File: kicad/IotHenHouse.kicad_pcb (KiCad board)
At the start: 2 copper layers, 55.9 x 80.9 mm, 60 parts, among them J1 GND NC 5V RXD TXD NC, J2 Conn_01x02_Female, J3 3.3V SW1 SW2, M1 + MOT -, SW0 RESET, SW1 FLASH, U1 LM7805_TO220, U2 ESP-12E, U3 L298P, U4 LM1117-3.3

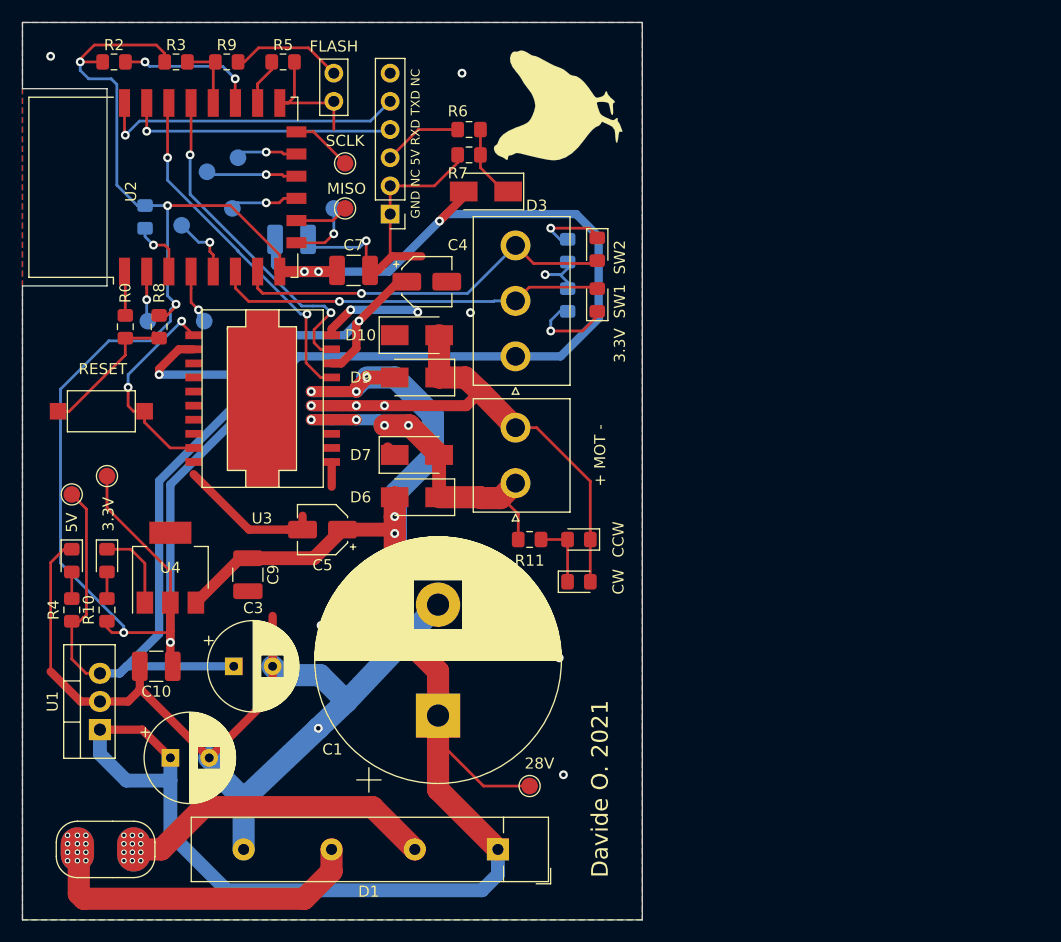
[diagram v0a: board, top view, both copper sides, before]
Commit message: mounting holes
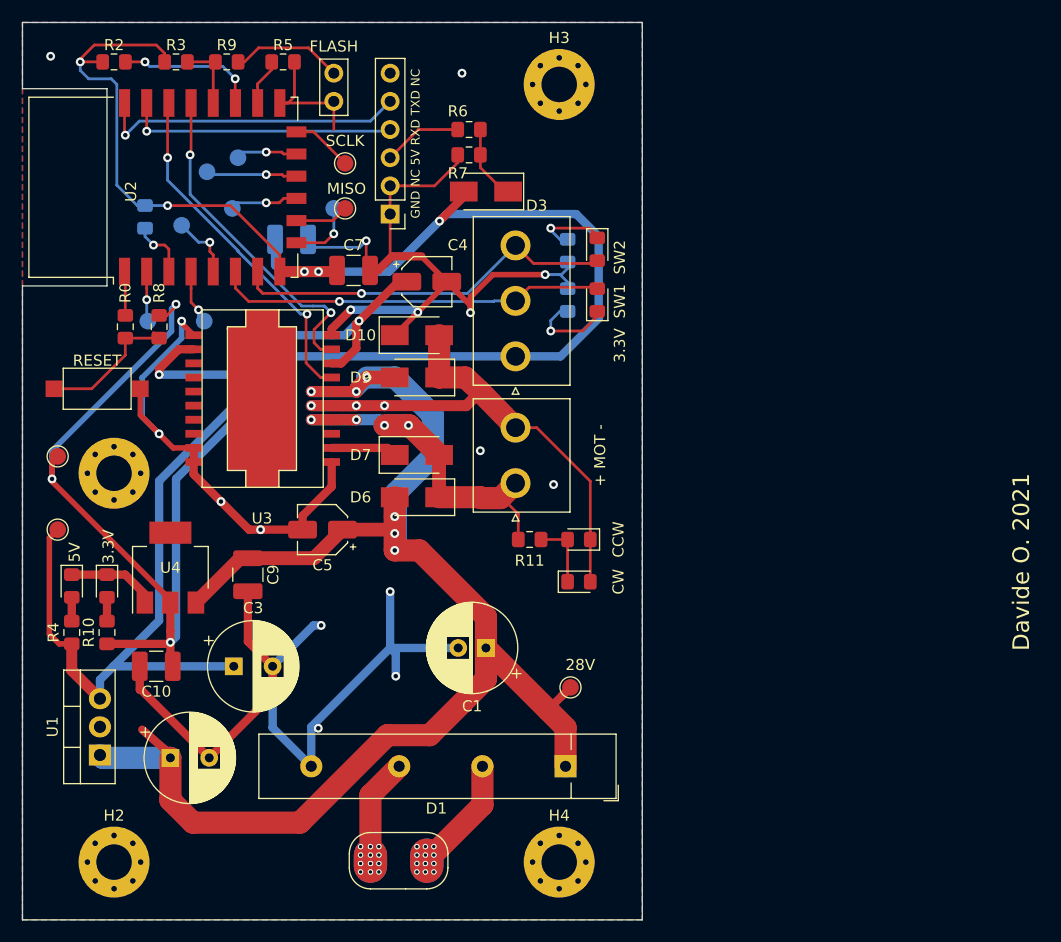
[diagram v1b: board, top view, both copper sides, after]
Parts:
- removed G***: LOGO, Logo:logo_hen_big
- removed G***: LOGO, Logo:logo_hen
- added H1: MountingHole, MountingHole:MountingHole_3.2mm_M3_Pad_Via, F.Cu at (43.2, 97.5)
- added H2: MountingHole, MountingHole:MountingHole_3.2mm_M3_Pad_Via, F.Cu at (43.2, 132.6)
- added H3: MountingHole, MountingHole:MountingHole_3.2mm_M3_Pad_Via, F.Cu at (83.3, 62.5)
- added H4: MountingHole, MountingHole:MountingHole_3.2mm_M3_Pad_Via, F.Cu at (83.3, 132.6)
- C1: footprint Capacitor_THT:CP_Radial_D22.0mm_P10.00mm_SnapIn -> Capacitor_THT:CP_Radial_D8.0mm_P2.50mm
- moved J2 26.4 mm to (68.8, 132.5) (x2)
- moved D1 9.66 mm to (84.8, 124.0)
- moved TP10 9.62 mm to (84.3, 116.8)
- moved C1 7.47 mm to (76.7, 113.3), turned to 180 degrees
- moved TP12 4.79 mm to (38.1, 96.0)
- moved TP11 3.42 mm to (38.1, 102.6)
- moved D2 2.29 mm to (39.4, 107.7)
- moved D8 2.29 mm to (42.5, 107.7)
- moved U1 2.29 mm to (41.9, 122.9)
- moved SW0 2.07 mm to (41.7, 89.9)
- moved R10 2.03 mm to (42.5, 111.9)
- moved R4 2.03 mm to (39.4, 111.9)
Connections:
- J1 pad 6: Net-(J1-Pad6) -> (no net)
- U3 pad 13: Net-(U3-Pad13) -> (no net)
- U3 pad 14: Net-(U3-Pad14) -> (no net)
- U3 pad 15: Net-(U3-Pad15) -> (no net)
- U3 pad 16: Net-(U3-Pad16) -> (no net)
- U3 pad 17: Net-(U3-Pad17) -> (no net)
- U3 pad 18: Net-(U3-Pad18) -> (no net)
- U3 pad 3: Net-(U3-Pad3) -> (no net)
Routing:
- net +3V3: track 231.0 -> 208.1 mm
- net VAC: track 30.0 -> 9.58 mm
- net GND: track 189.6 -> 209.8 mm, vias 13 -> 17
- net +28V: track 162.0 -> 142.1 mm
- net Net-(D1-Pad4): track 28.4 -> 10.6 mm

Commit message: logos
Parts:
- added G***: LOGO, logo:logo_hen, F.Cu at (65.0, 112.3)
- added G***: LOGO, logo:logo_hen_big, B.Cu at (62.0, 108.2)

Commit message: last commit for version 1.0
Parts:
- removed G***: LOGO, logo:logo_hen
- removed G***: LOGO, logo:logo_hen_big
- moved TP12 16.8 mm to (53.6, 102.6)
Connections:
- C9 pad 1: +28V -> +5V
- U4 pad 3: +28V -> +5V
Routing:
- net GND: track 209.8 -> 165.5 mm
- net +3V3: track 208.1 -> 228.5 mm, vias 8 -> 9
- net +28V: track 142.1 -> 122.7 mm
- net +5V: track 98.4 -> 105.1 mm, vias 2 -> 4
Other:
- outline, holes or cut-outs redrawn
- board text added: "Davide O. 2021 gtihub/Dadigno"
